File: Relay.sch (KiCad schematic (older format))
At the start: 0 parts

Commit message: Module 3. Unit 5
Relay Block
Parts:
- added D?: DIODE, ~, symbol DIODE
- added D?: LED, ~, symbol LED
- added K?: SPDT, ~, symbol SPDT
- added Q?: NPN, ~, symbol NPN
- added R? (x6): R, ~, symbol R
- added U?: PHTRANS, ~, symbol PHTRANS
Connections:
- net labels added: +12V, COM, GND, NC, NO
- net labels removed: Relay +, Relay -
- wire segments 0 -> 25
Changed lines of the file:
@@
 LIBS:contrib
 LIBS:valves
+LIBS:BenchBudEE_Michael_James
 LIBS:BenchBudEE_Michael_James-cache
 EELAYER 27 0
@@
 Comment4 ""
 $EndDescr
-Text HLabel 3150 3450 0    60   Input ~ 0
+Text HLabel 3200 3900 0    60   Input ~ 0
 DIN +
-Text HLabel 3100 3750 0    60   Output ~ 0
+Text HLabel 3200 4250 0    60   Output ~ 0
 DN -
-Text HLabel 7900 3450 0    60   Input ~ 0
-Relay +
-Text HLabel 7850 3800 0    60   Output ~ 0
-Relay -
+Text HLabel 10450 3050 2    60   BiDi ~ 0
+NC
+Text HLabel 10450 3250 2    60   BiDi ~ 0
+NO
+$Comp
+L PHTRANS U?
+U 1 1 52F868D5
+P 5150 4100
+F 0 "U?" H 5100 4450 70  0000 C CNN
+F 1 "PHTRANS" H 5100 3750 70  0000 C CNN
+F 2 "~" H 5150 4100 60  0000 C CNN
+F 3 "~" H 5150 4100 60  0000 C CNN
+	1    5150 4100
+	1    0    0    -1
+$EndComp
+$Comp
+L R R?
+U 1 1 52F868F3
+P 7000 4300
+F 0 "R?" V 7080 4300 40  0000 C CNN
+F 1 "R" V 7007 4301 40  0000 C CNN
+F 2 "~" V 6930 4300 30  0000 C CNN
+F 3 "~" H 7000 4300 30  0000 C CNN
+	1    7000 4300
+	0    -1   -1   0
+$EndComp
+$Comp
+L NPN Q?
+U 1 1 52F86911
+P 8900 4300
+F 0 "Q?" H 8900 4150 50  0000 R CNN
+F 1 "NPN" H 8900 4450 50  0000 R CNN
+F 2 "~" H 8900 4300 60  0000 C CNN
+F 3 "~" H 8900 4300 60  0000 C CNN
+	1    8900 4300
+	1    0    0    -1
+$EndComp
+$Comp
+L LED D?
+U 1 1 52F86920
+P 6500 4700
+F 0 "D?" H 6500 4800 50  0000 C CNN
+F 1 "LED" H 6500 4600 50  0000 C CNN
+F 2 "~" H 6500 4700 60  0000 C CNN
+F 3 "~" H 6500 4700 60  0000 C CNN
+	1    6500 4700
+	0    1    1    0
+$EndComp
+$Comp
+L SPDT K?
+U 1 1 52F84FBF
+P 9500 3100
+F 0 "K?" H 9500 3400 70  0000 C CNN
+F 1 "SPDT" H 9500 2550 70  0000 C CNN
+F 2 "~" H 9500 3100 60  0000 C CNN
+F 3 "~" H 9500 3100 60  0000 C CNN
+	1    9500 3100
+	1    0    0    -1
+$EndComp
+Text HLabel 10450 2550 2    60   BiDi ~ 0
+COM
+Wire Wire Line
+	8550 3150 9100 3150
+Wire Wire Line
+	9900 3050 10450 3050
+Wire Wire Line
+	10450 3250 9900 3250
+Wire Wire Line
+	5700 4300 6750 4300
+Wire Wire Line
+	6650 3350 9100 3350
+Wire Wire Line
+	6650 3050 6650 4100
+$Comp
+L R R?
+U 1 1 52F854DC
+P 9000 5050
+F 0 "R?" V 9080 5050 40  0000 C CNN
+F 1 "R" V 9007 5051 40  0000 C CNN
+F 2 "~" V 8930 5050 30  0000 C CNN
+F 3 "~" H 9000 5050 30  0000 C CNN
+	1    9000 5050
+	-1   0    0    1
+$EndComp
+$Comp
+L GND #PWR?
+U 1 1 52F854EE
+P 9000 5900
+F 0 "#PWR?" H 9000 5900 30  0001 C CNN
+F 1 "GND" H 9000 5830 30  0001 C CNN
+F 2 "" H 9000 5900 60  0000 C CNN
+F 3 "" H 9000 5900 60  0000 C CNN
+	1    9000 5900
+	1    0    0    -1
+$EndComp
+$Comp
+L R R?
+U 1 1 52F85643
+P 6500 5400
+F 0 "R?" V 6580 5400 40  0000 C CNN
+F 1 "R" V 6507 5401 40  0000 C CNN
+F 2 "~" V 6430 5400 30  0000 C CNN
+F 3 "~" H 6500 5400 30  0000 C CNN
+	1    6500 5400
+	-1   0    0    1
+$EndComp
+Wire Wire Line
+	6500 4300 6500 4500
+Connection ~ 6500 4300
+Wire Wire Line
+	6500 4900 6500 5150
+$Comp
+L R R?
+U 1 1 52F85663
+P 6650 2800
+F 0 "R?" V 6730 2800 40  0000 C CNN
+F 1 "R" V 6657 2801 40  0000 C CNN
+F 2 "~" V 6580 2800 30  0000 C CNN
+F 3 "~" H 6650 2800 30  0000 C CNN
+	1    6650 2800
+	-1   0    0    1
+$EndComp
+$Comp
+L +12V #PWR?
+U 1 1 52F8567A
+P 6650 2400
+F 0 "#PWR?" H 6650 2350 20  0001 C CNN
+F 1 "+12V" H 6650 2500 30  0000 C CNN
+F 2 "" H 6650 2400 60  0000 C CNN
+F 3 "" H 6650 2400 60  0000 C CNN
+	1    6650 2400
+	1    0    0    -1
+$EndComp
+Wire Wire Line
+	6650 2400 6650 2550
+Wire Wire Line
+	6500 5650 9000 5650
+Wire Wire Line
+	6650 4100 5700 4100
+Connection ~ 6650 3750
+$Comp
+L R R?
+U 1 1 52F856D2
+P 6100 3900
+F 0 "R?" V 6180 3900 40  0000 C CNN
+F 1 "R" V 6107 3901 40  0000 C CNN
+F 2 "~" V 6030 3900 30  0000 C CNN
+F 3 "~" H 6100 3900 30  0000 C CNN
+	1    6100 3900
+	0    -1   -1   0
+$EndComp
+Wire Wire Line
+	5700 3900 5850 3900
+Wire Wire Line
+	6350 3900 6650 3900
+Connection ~ 6650 3900
+$Comp
+L R R?
+U 1 1 52F8570B
+P 4000 4250
+F 0 "R?" V 4080 4250 40  0000 C CNN
+F 1 "R" V 4007 4251 40  0000 C CNN
+F 2 "~" V 3930 4250 30  0000 C CNN
+F 3 "~" H 4000 4250 30  0000 C CNN
+	1    4000 4250
+	0    -1   -1   0
+$EndComp
+Wire Wire Line
+	4600 3900 3200 3900
+Wire Wire Line
+	3200 4250 3750 4250
+Wire Wire Line
+	4250 4250 4600 4250
+Wire Wire Line
+	8550 3150 8550 2550
+Wire Wire Line
+	8550 2550 10450 2550
+Wire Wire Line
+	7250 4300 8700 4300
+Wire Wire Line
+	9000 4500 9000 4800
+Wire Wire Line
+	9000 5300 9000 5900
+Connection ~ 9000 5650
+Wire Wire Line
+	9100 3450 9000 3450
+Wire Wire Line
+	9000 3450 9000 4100
+$Comp
+L DIODE D?
+U 1 1 52F8597A
+P 8150 3700
+F 0 "D?" H 8150 3800 40  0000 C CNN
+F 1 "DIODE" H 8150 3600 40  0000 C CNN
+F 2 "~" H 8150 3700 60  0000 C CNN
+F 3 "~" H 8150 3700 60  0000 C CNN
+	1    8150 3700
+	0    -1   -1   0
+$EndComp
+Wire Wire Line
+	8150 3350 8150 3500
+Connection ~ 8150 3350
+Wire Wire Line
+	8150 3900 9000 3900
+Connection ~ 9000 3900
 $EndSCHEMATC

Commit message: M3 U5
Power protection and filtering
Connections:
- net labels added: +12P
- net labels removed: +12V
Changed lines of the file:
@@
 $Descr A4 11693 8268
 encoding utf-8
-Sheet 4 8
+Sheet 4 9
 Title ""
-Date "10 feb 2014"
+Date "12 feb 2014"
 Rev ""
 Comp ""
@@
 	-1   0    0    1
 $EndComp
-$Comp
-L +12V #PWR?
-U 1 1 52F8567A
-P 6650 2400
-F 0 "#PWR?" H 6650 2350 20  0001 C CNN
-F 1 "+12V" H 6650 2500 30  0000 C CNN
-F 2 "" H 6650 2400 60  0000 C CNN
-F 3 "" H 6650 2400 60  0000 C CNN
-	1    6650 2400
-	1    0    0    -1
-$EndComp
 Wire Wire Line
 	6650 2400 6650 2550
@@
 	8150 3900 9000 3900
 Connection ~ 9000 3900
+$Comp
+L +12P #PWR?
+U 1 1 52FB0F57
+P 6650 2400
+F 0 "#PWR?" H 6650 2370 30  0001 C CNN
+F 1 "+12P" H 6650 2500 30  0000 C CNN
+F 2 "" H 6650 2400 60  0000 C CNN
+F 3 "" H 6650 2400 60  0000 C CNN
+	1    6650 2400
+	1    0    0    -1
+$EndComp
 $EndSCHEMATC

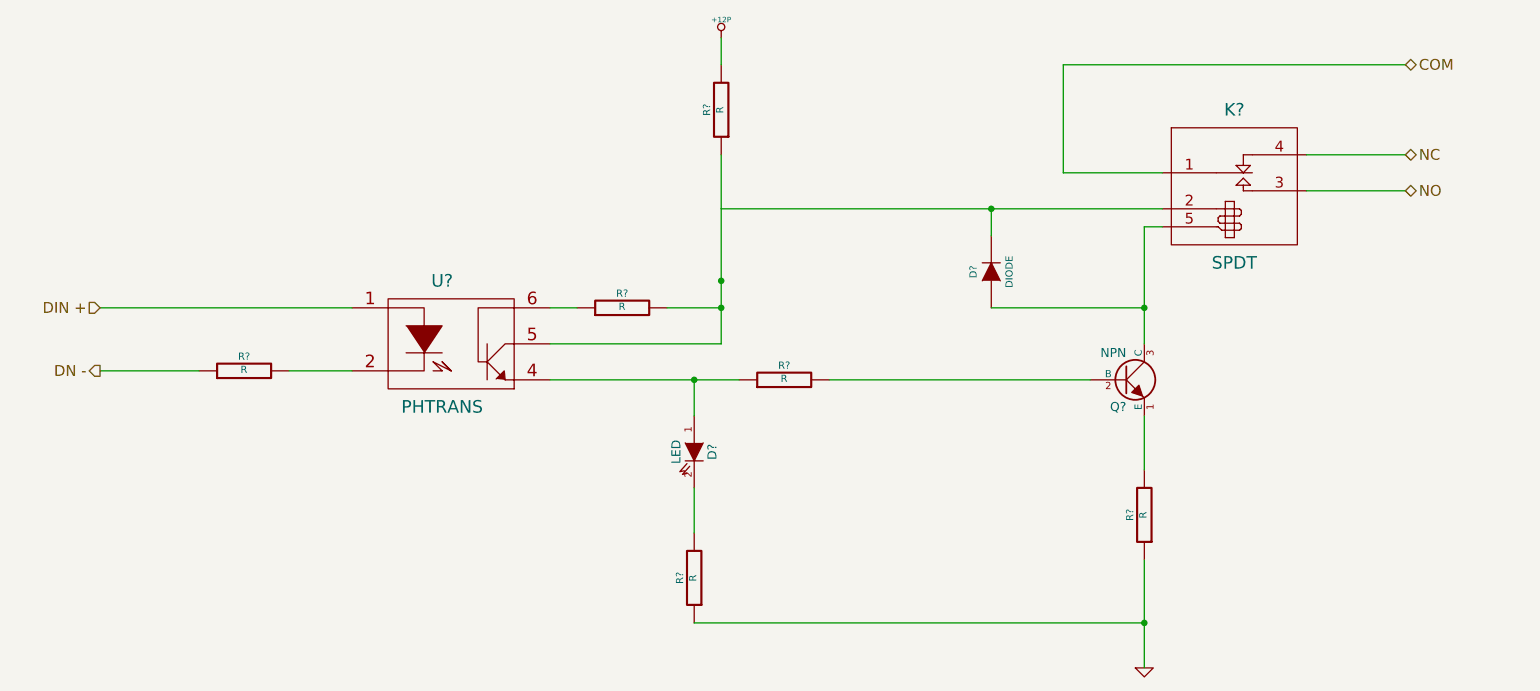
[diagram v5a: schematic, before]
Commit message: M3 U8
Arduino Module.   My Arduino Pin numbering does not matches Chris'.  I
believe he missed one in the video
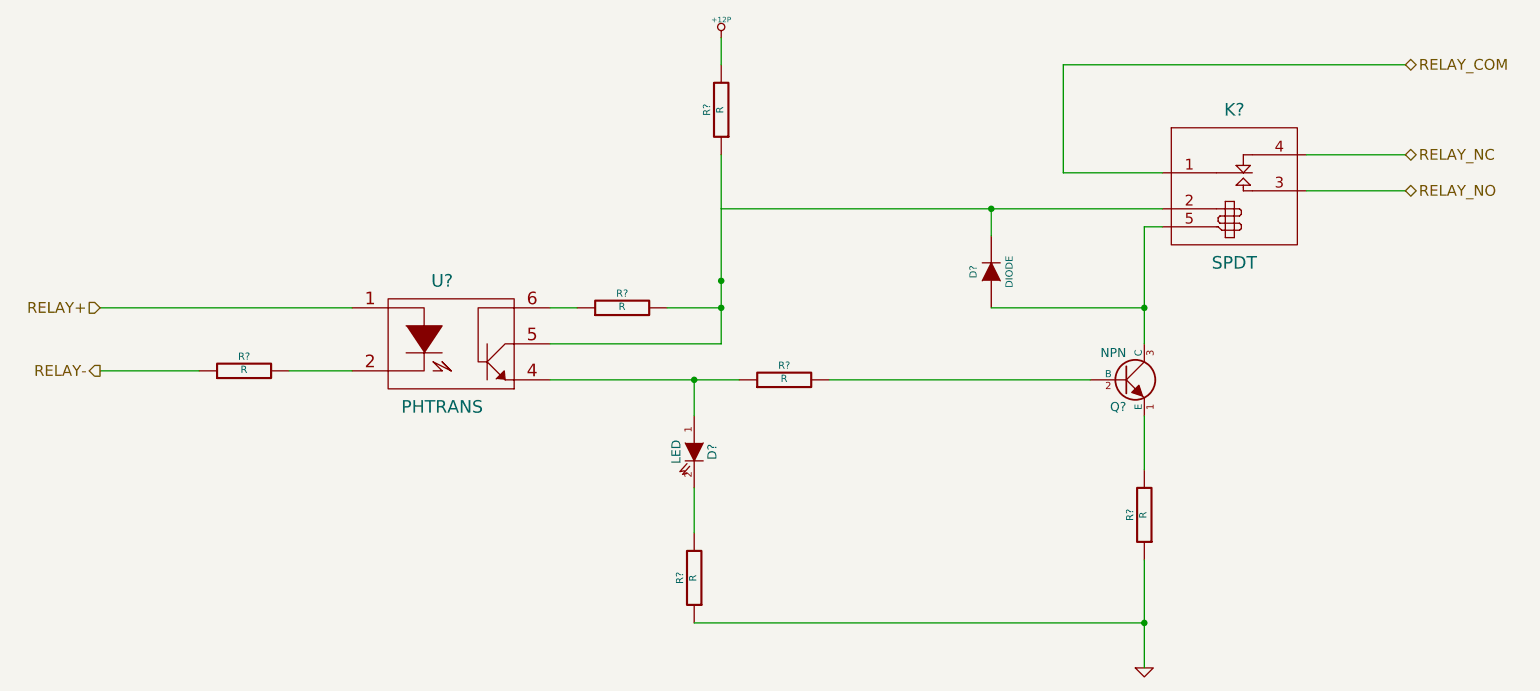
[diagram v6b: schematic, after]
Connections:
- net labels added: RELAY+, RELAY-, RELAY_COM, RELAY_NC, RELAY_NO
- net labels removed: COM, DIN +, DN -, NC, NO
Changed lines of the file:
@@
 Sheet 4 9
 Title ""
-Date "14 feb 2014"
+Date "15 feb 2014"
 Rev ""
 Comp ""
@@
 $EndDescr
 Text HLabel 3200 3900 0    60   Input ~ 0
-DIN +
+RELAY+
 Text HLabel 3200 4250 0    60   Output ~ 0
-DN -
+RELAY-
 Text HLabel 10450 3050 2    60   BiDi ~ 0
-NC
+RELAY_NC
 Text HLabel 10450 3250 2    60   BiDi ~ 0
-NO
+RELAY_NO
 $Comp
 L PHTRANS U?
@@
 $EndComp
 Text HLabel 10450 2550 2    60   BiDi ~ 0
-COM
+RELAY_COM
 Wire Wire Line
 	8550 3150 9100 3150
